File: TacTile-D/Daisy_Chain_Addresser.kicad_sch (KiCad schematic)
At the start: 9 parts, among them U10 74LVC1G18, U14 74LVC2G00, U15 74LVC2G32, U16 74LS74, U17 74LVC1G373, U18 74LVC2G04, U20 74AUC1G74, U6 74LVC2G08, U7 74LVC1G18

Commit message: Mounted ICs without sockets to save space
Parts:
- U10, U17, U18, U7: footprint Package_DIP:DIP-6_W7.62mm_Socket -> Package_DIP:DIP-6_W7.62mm
- U14, U15, U20, U6: footprint Package_DIP:DIP-8_W7.62mm_Socket -> Package_DIP:DIP-8_W7.62mm
- U16: footprint Package_DIP:DIP-14_W7.62mm_Socket -> Package_DIP:DIP-14_W7.62mm
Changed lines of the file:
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@@
       (effects (font (size 1.27 1.27)) (justify left))
     )
-    (property "Footprint" "Package_DIP:DIP-6_W7.62mm_Socket" (at 267.97 43.18 0)
+    (property "Footprint" "Package_DIP:DIP-6_W7.62mm" (at 267.97 43.18 0)
       (effects (font (size 1.27 1.27)) hide)
     )
@@
       (effects (font (size 1.27 1.27)) (justify left))
     )
-    (property "Footprint" "Package_DIP:DIP-14_W7.62mm_Socket" (at 57.15 69.85 0)
+    (property "Footprint" "Package_DIP:DIP-14_W7.62mm" (at 57.15 69.85 0)
       (effects (font (size 1.27 1.27)) hide)
     )
@@
       (effects (font (size 1.27 1.27)))
     )
-    (property "Footprint" "Package_DIP:DIP-6_W7.62mm_Socket" (at 137.16 76.2 0)
+    (property "Footprint" "Package_DIP:DIP-6_W7.62mm" (at 137.16 76.2 0)
       (effects (font (size 1.27 1.27)) hide)
     )
@@
       (effects (font (size 1.27 1.27)) (justify left))
     )
-    (property "Footprint" "Package_DIP:DIP-14_W7.62mm_Socket" (at 114.3 34.29 0)
+    (property "Footprint" "Package_DIP:DIP-14_W7.62mm" (at 114.3 34.29 0)
       (effects (font (size 1.27 1.27)) hide)
     )
@@
       (effects (font (size 1.27 1.27)))
     )
-    (property "Footprint" "Package_DIP:DIP-8_W7.62mm_Socket" (at 114.3 99.06 0)
+    (property "Footprint" "Package_DIP:DIP-8_W7.62mm" (at 114.3 99.06 0)
       (effects (font (size 1.27 1.27)) hide)
     )
@@
       (effects (font (size 1.27 1.27)) (justify left))
     )
-    (property "Footprint" "Package_DIP:DIP-6_W7.62mm_Socket" (at 114.3 62.23 0)
+    (property "Footprint" "Package_DIP:DIP-6_W7.62mm" (at 114.3 62.23 0)
       (effects (font (size 1.27 1.27)) hide)
     )
@@
       (effects (font (size 1.27 1.27)) (justify right))
     )
-    (property "Footprint" "Package_DIP:DIP-8_W7.62mm_Socket" (at 57.15 90.17 0)
+    (property "Footprint" "Package_DIP:DIP-8_W7.62mm" (at 57.15 90.17 0)
       (effects (font (size 1.27 1.27)) hide)
     )
@@
       (effects (font (size 1.27 1.27)) (justify left))
     )
-    (property "Footprint" "Package_DIP:DIP-8_W7.62mm_Socket" (at 27.94 36.83 0)
+    (property "Footprint" "Package_DIP:DIP-8_W7.62mm" (at 27.94 36.83 0)
       (effects (font (size 1.27 1.27)) hide)
     )
@@
       (effects (font (size 1.27 1.27)))
     )
-    (property "Footprint" "Package_DIP:DIP-6_W7.62mm_Socket" (at 36.83 67.31 0)
+    (property "Footprint" "Package_DIP:DIP-6_W7.62mm" (at 36.83 67.31 0)
       (effects (font (size 1.27 1.27)) hide)
     )
@@
       (effects (font (size 1.27 1.27)))
     )
-    (property "Footprint" "Package_DIP:DIP-8_W7.62mm_Socket" (at 88.9 104.14 0)
+    (property "Footprint" "Package_DIP:DIP-8_W7.62mm" (at 88.9 104.14 0)
       (effects (font (size 1.27 1.27)) hide)
     )
@@
       (effects (font (size 1.27 1.27)) (justify right))
     )
-    (property "Footprint" "Package_DIP:DIP-6_W7.62mm_Socket" (at 21.59 90.17 0)
+    (property "Footprint" "Package_DIP:DIP-6_W7.62mm" (at 21.59 90.17 0)
       (effects (font (size 1.27 1.27)) hide)
     )
@@
       (effects (font (size 1.27 1.27)))
     )
-    (property "Footprint" "Package_DIP:DIP-8_W7.62mm_Socket" (at 267.97 73.66 0)
+    (property "Footprint" "Package_DIP:DIP-8_W7.62mm" (at 267.97 73.66 0)
       (effects (font (size 1.27 1.27)) hide)
     )
@@
       (effects (font (size 1.27 1.27)))
     )
-    (property "Footprint" "Package_DIP:DIP-8_W7.62mm_Socket" (at 101.6 26.67 0)
+    (property "Footprint" "Package_DIP:DIP-8_W7.62mm" (at 101.6 26.67 0)
       (effects (font (size 1.27 1.27)) hide)
     )
@@
       (effects (font (size 1.27 1.27)))
     )
-    (property "Footprint" "Package_DIP:DIP-14_W7.62mm_Socket" (at 267.97 24.13 0)
+    (property "Footprint" "Package_DIP:DIP-14_W7.62mm" (at 267.97 24.13 0)
       (effects (font (size 1.27 1.27)) hide)
     )
@@
       (effects (font (size 1.27 1.27)))
     )
-    (property "Footprint" "Package_DIP:DIP-8_W7.62mm_Socket" (at 267.97 90.17 0)
+    (property "Footprint" "Package_DIP:DIP-8_W7.62mm" (at 267.97 90.17 0)
       (effects (font (size 1.27 1.27)) hide)
     )
@@
       (effects (font (size 1.27 1.27)) (justify left))
     )
-    (property "Footprint" "Package_DIP:DIP-6_W7.62mm_Socket" (at 267.97 57.15 0)
+    (property "Footprint" "Package_DIP:DIP-6_W7.62mm" (at 267.97 57.15 0)
       (effects (font (size 1.27 1.27)) hide)
     )
@@
       (effects (font (size 1.27 1.27)))
     )
-    (property "Footprint" "Package_DIP:DIP-8_W7.62mm_Socket" (at 73.66 24.13 0)
-      (effects (font (size 1.27 1.27)) hide)
-    )
+    (property "Footprint" "Package_DIP:DIP-8_W7.62mm" (at 73.66 24.13 0)
+      (effects (font (size 1.27 1.27)) hide)
+    )

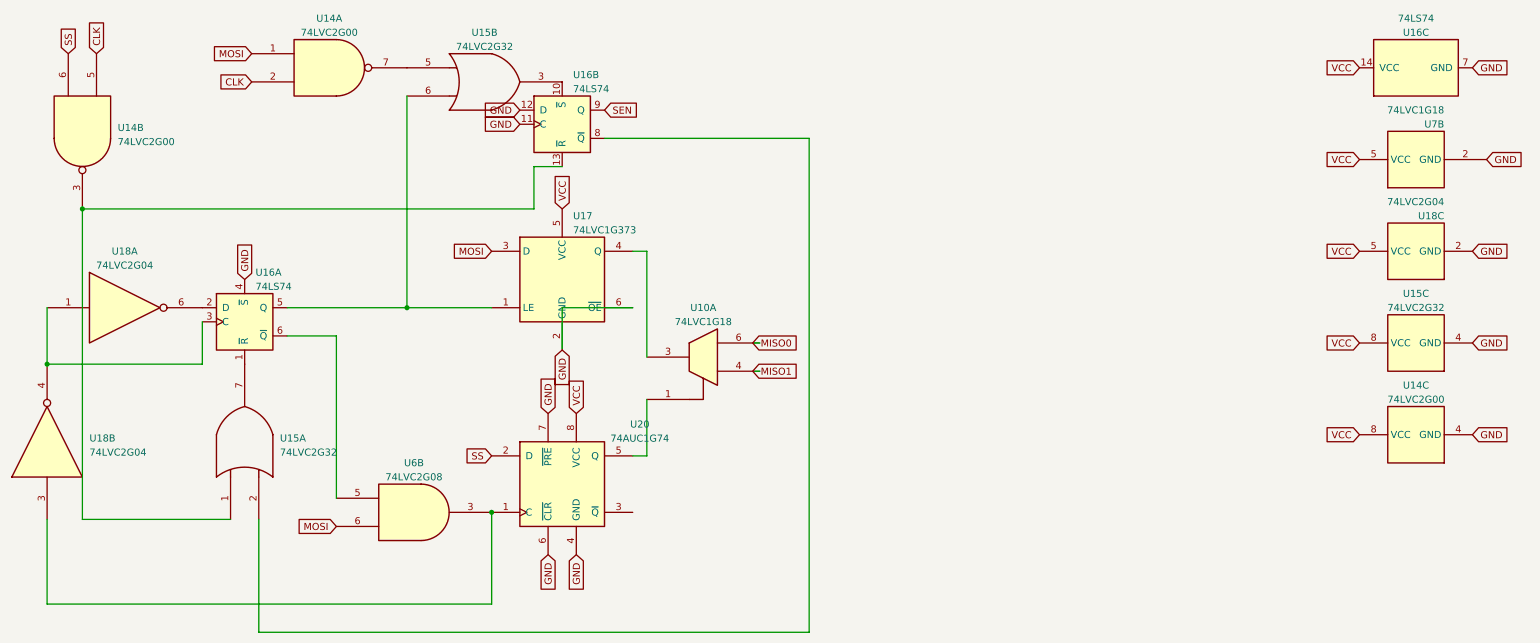
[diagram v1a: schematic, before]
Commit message: Updated D schematic to reflect available ICs
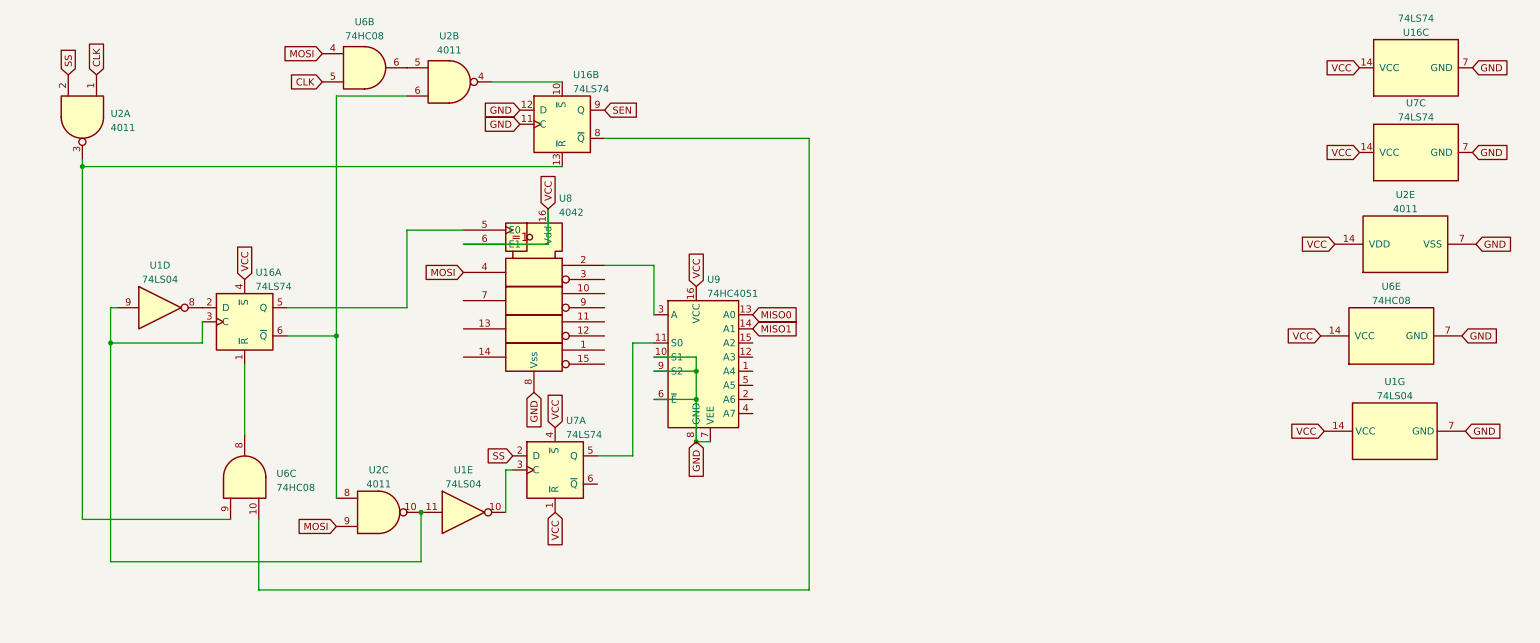
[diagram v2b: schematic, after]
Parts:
- removed U10, U7: 74LVC1G18, Package_DIP:DIP-6_W7.62mm, symbol 74xGxx:74LVC1G18
- removed U14: 74LVC2G00, Package_DIP:DIP-8_W7.62mm, symbol 74xGxx:74LVC2G00
- removed U15: 74LVC2G32, Package_DIP:DIP-8_W7.62mm, symbol 74xGxx:74LVC2G32
- removed U17: 74LVC1G373, Package_DIP:DIP-6_W7.62mm, symbol 74xGxx:74LVC1G373
- removed U18: 74LVC2G04, Package_DIP:DIP-6_W7.62mm, symbol 74xGxx:74LVC2G04
- removed U20: 74AUC1G74, Package_DIP:DIP-8_W7.62mm, symbol 74xGxx:74AUC1G74
- removed U6: 74LVC2G08, Package_DIP:DIP-8_W7.62mm, symbol 74xGxx:74LVC2G08
- added U1: 74LS04, Package_DIP:DIP-14_W7.62mm, symbol 74xx:74LS04
- added U2: 4011, Package_DIP:DIP-14_W7.62mm, symbol 4xxx:4011
- added U6: 74HC08, symbol TacTile:74HC08
- added U7: 74LS74, Package_DIP:DIP-14_W7.62mm, symbol 74xx:74LS74
- added U8: 4042, Package_DIP:DIP-16_W7.62mm, symbol 4xxx_IEEE:4042
- added U9: 74HC4051, Package_DIP:DIP-16_W7.62mm, symbol 74xx:74HC4051
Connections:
- net CLK: now also U2.1, U6.5
- net GND: now also U1.7 (GND), U2.7 (VSS), U6.7 (GND), U7.7 (GND), U8.8 (Vss), U9.10 (S1), U9.6 (~{E}), U9.7 (VEE), U9.8 (GND), U9.9 (S2); no longer U16.4 (~{S})
- net MISO0: now also U9.13 (A0)
- net MISO1: now also U9.14 (A1)
- net MOSI: now also U2.9, U6.4, U8.4
- net SS: now also U2.2, U7.2 (D)
- net VCC: now also U16.4 (~{S}), U1.14 (VCC), U2.14 (VDD), U6.14 (VCC), U7.1 (~{R}), U7.14 (VCC), U7.4 (~{S}), U8.16 (Vdd), U8.6 (E1), U9.16 (VCC)
- net at U16.1 (~{R}): now also U6.8
- net at U16.2 (D): now also U1.8
- net at U16.3 (C): now also U1.11, U1.9, U2.10
- net at U16.5 (Q): now also U8.5 (E0)
- net at U16.6 (~{Q}): now also U2.6, U2.8
- net at U16.10 (~{S}): now also U2.4
- net at U16.13 (~{R}): now also U2.3, U6.9
- net at U16.8 (~{Q}): now also U6.10
- new net: U2.5, U6.6
- new net: U1.10, U7.3 (C)
- new net: U7.5 (Q), U9.11 (S0)
- new net: U8.2, U9.3 (A)

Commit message: Checked new board D spacing requirements
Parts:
- U6: footprint (none) -> Package_DIP:DIP-14_W7.62mm
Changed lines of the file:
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@@
       (effects (font (size 1.27 1.27)))
     )
-    (property "Footprint" "" (at 78.74 24.13 0)
+    (property "Footprint" "Package_DIP:DIP-14_W7.62mm" (at 78.74 24.13 0)
       (effects (font (size 1.27 1.27)) hide)
     )
@@
       (effects (font (size 1.27 1.27)))
     )
-    (property "Footprint" "" (at 263.525 72.39 0)
+    (property "Footprint" "Package_DIP:DIP-14_W7.62mm" (at 263.525 72.39 0)
       (effects (font (size 1.27 1.27)) hide)
     )
@@
       (effects (font (size 1.27 1.27)) (justify right))
     )
-    (property "Footprint" "" (at 57.15 97.79 0)
-      (effects (font (size 1.27 1.27)) hide)
-    )
+    (property "Footprint" "Package_DIP:DIP-14_W7.62mm" (at 57.15 97.79 0)
+      (effects (font (size 1.27 1.27)) hide)
+    )

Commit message: Fixed issues with D board and rerouted
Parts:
- removed U8: 4042, Package_DIP:DIP-16_W7.62mm, symbol 4xxx_IEEE:4042
- added unit 3 of U1
- added unit 4 of U6
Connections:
- net GND: no longer U16.11 (C), U16.12 (D)
- net MOSI: now also U6.13
- net VCC: now also U16.10 (~{S})
- net at U16.5 (Q): now also U6.12
- net at U2.4: now also U1.5; no longer U16.10 (~{S})
- net at U9.3 (A): now also U6.11
- new net: U1.6, U16.12 (D)
- new net ACLK: U16.11 (C)
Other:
- moved on the sheet: U16B, U2A
